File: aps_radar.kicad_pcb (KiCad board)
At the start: 4 copper layers, 122.9 x 53.5 mm, 339 parts, among them J1 TRIG_MUX_OUT, J10 RX3_RX4, J2 RX1_RX2, J3 POWER_IN, J4 Tx_Ant, J5 Rx1_Ant, J6 Rx2_Ant, J7 Rx3_Ant, J8 Rx4_Ant, J9 LMX2491_CONN, SW1 PA_EN, SW2 ON/OFF, U1 HMC717A, U10 HMC951A, U11 OPA192, U12 OPA192, U13 HMC717A, U14 HMC951A, U15 OPA192, U16 OPA192, U17 HMC540S, U18 ASDMB-100MHz, U19 OPA192, U2 HMC951A, U20 HMC431, U21 TQP5523, U22 LMX2491RTWR, U23 LP5900-TL3.3, U24 TPS82140, U25 TPS7A49, U26 LP5900-TL3.0, U27 TPS7A90, U28 TPS7A92, U3 OPA192, U4 OPA192, U5 HMC717A, U6 HMC951A, U7 OPA192, U8 OPA192, U9 HMC717A

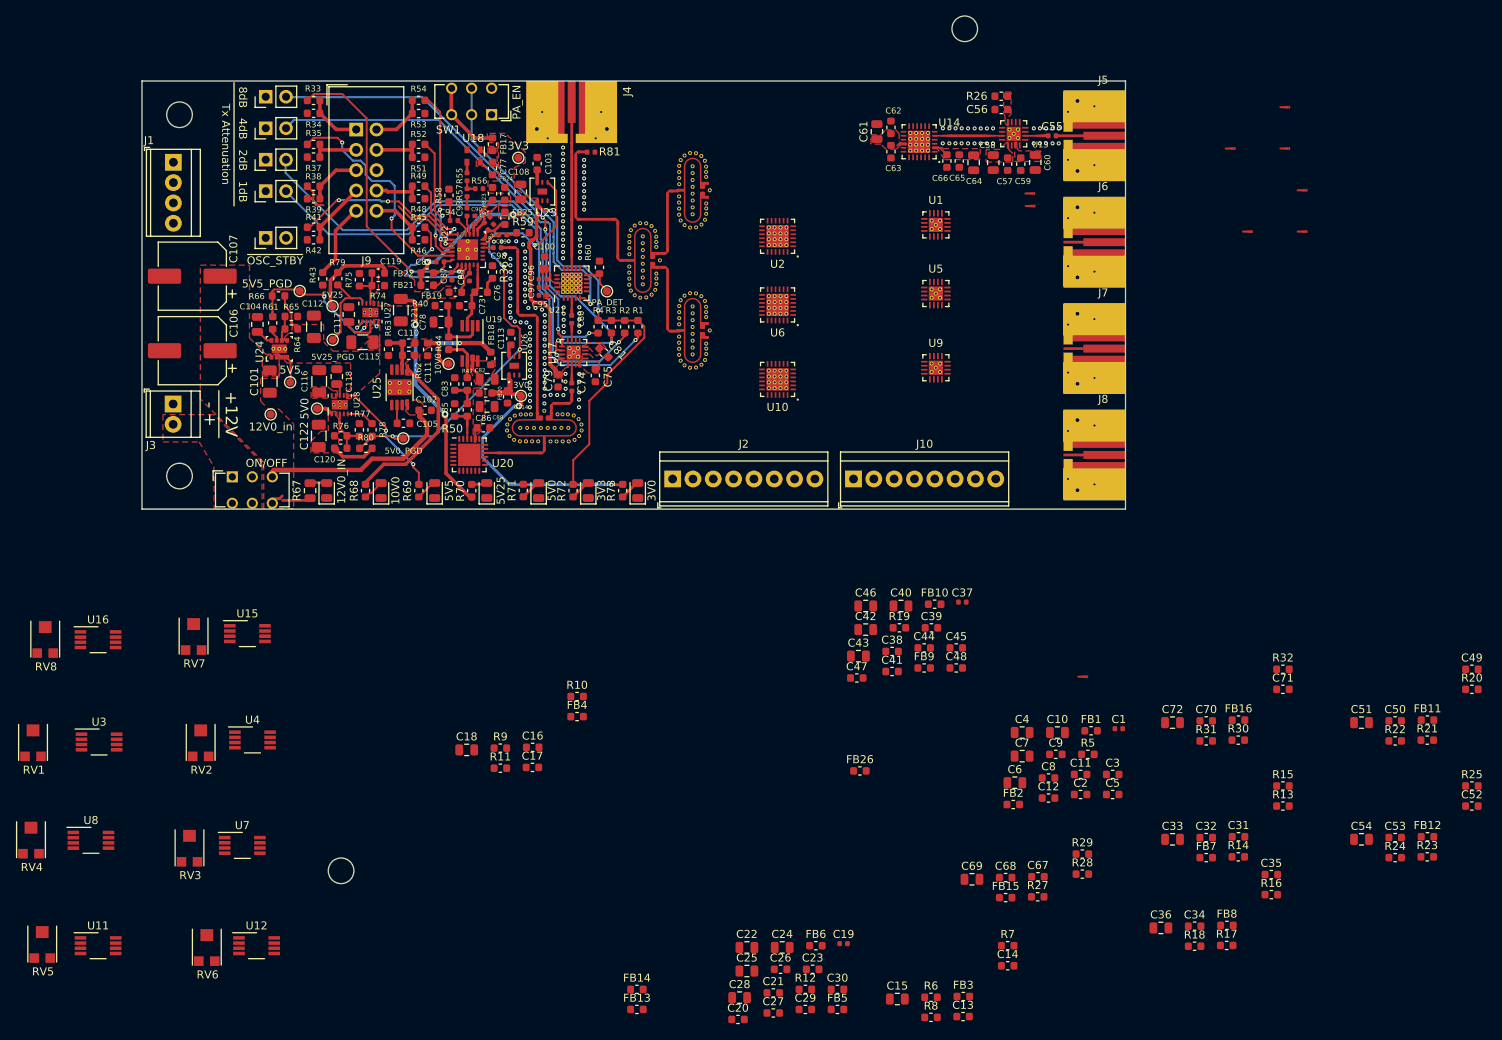
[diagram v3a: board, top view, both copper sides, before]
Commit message: Finished placing parts
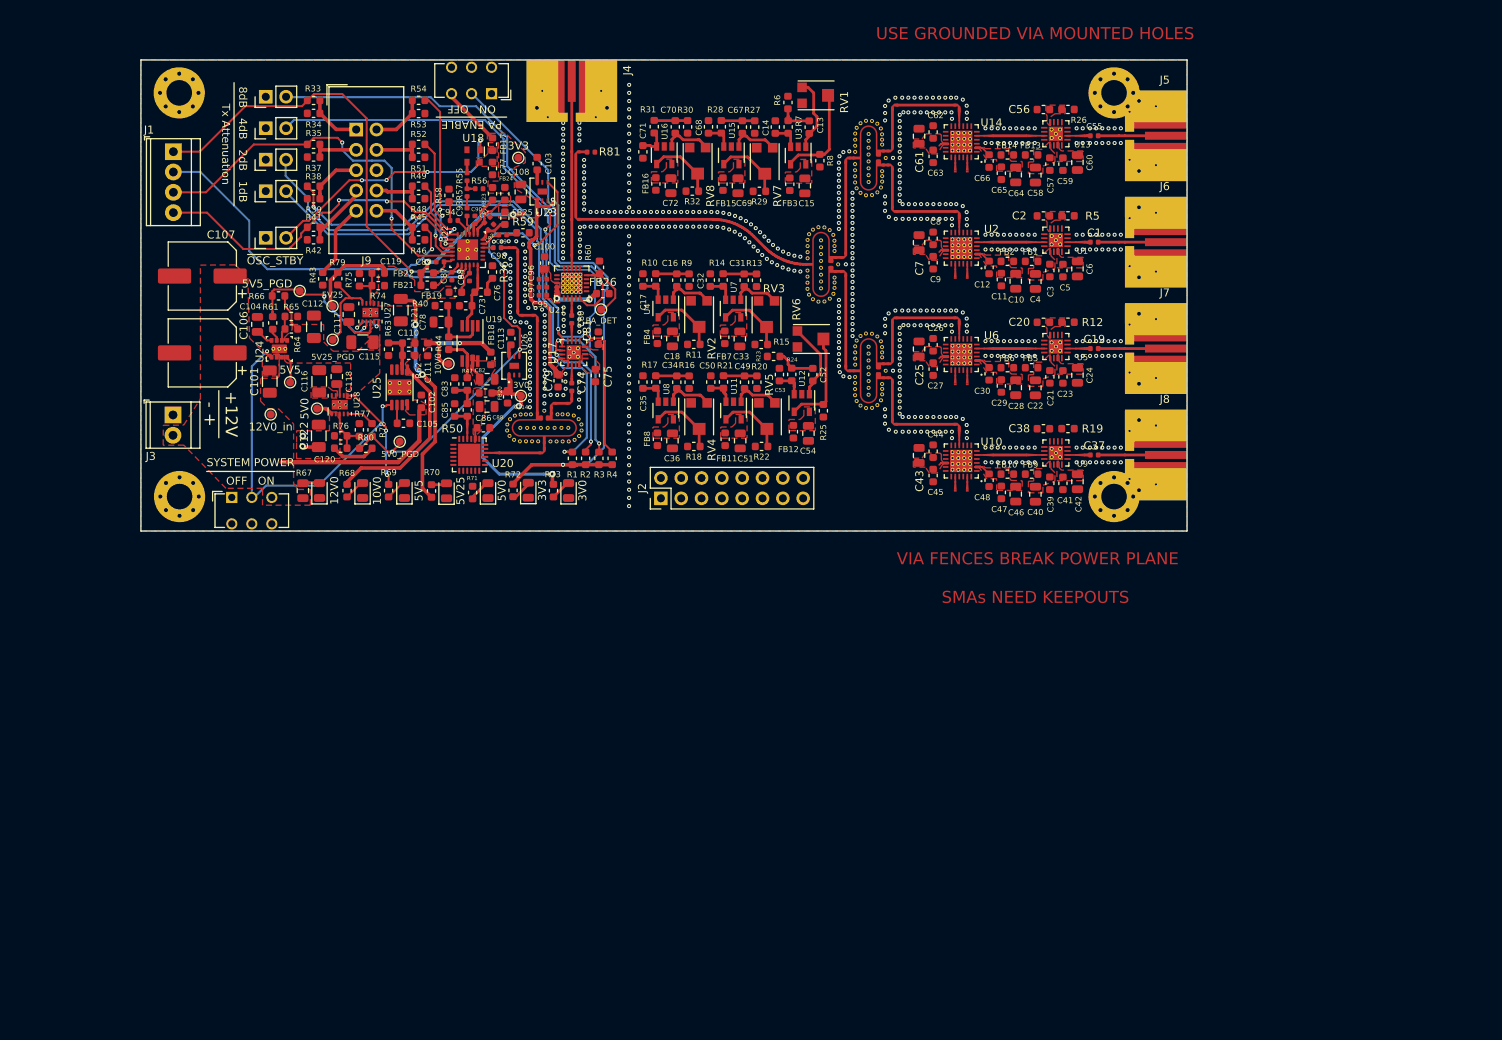
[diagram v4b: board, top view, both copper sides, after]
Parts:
- removed J10: RX3_RX4, TerminalBlock_TE-Connectivity:TerminalBlock_TE_282834-8_1x08_P2.54mm_Horizontal
- added TL37: ic_taper, aps_radar_lib:IC_Taper_0.22_0.35, F.Cu at (198.3, 41.6)
- added TL38: ic_taper, aps_radar_lib:IC_Taper_0.22_0.35, F.Cu at (198.8, 48.7)
- added TL39: ic_taper, aps_radar_lib:IC_Taper_0.22_0.35, F.Cu at (199.8, 54.9)
- added TL40: ic_taper, aps_radar_lib:IC_Taper_0.22_0.35, F.Cu at (198.3, 54.9)
- added TL41: ic_taper, aps_radar_lib:IC_Taper_0.22_0.35, F.Cu at (198.8, 62.0)
- added TL42: ic_taper, aps_radar_lib:IC_Taper_0.22_0.35, F.Cu at (199.8, 68.2)
- added TL43: ic_taper, aps_radar_lib:IC_Taper_0.22_0.35, F.Cu at (198.3, 68.2)
- added TL44: ic_taper, aps_radar_lib:IC_Taper_0.22_0.35, F.Cu at (198.8, 22.1)
- added TL45: ic_taper, aps_radar_lib:IC_Taper_0.22_0.35, F.Cu at (199.8, 28.3)
- added TL46: ic_taper, aps_radar_lib:IC_Taper_0.22_0.35, F.Cu at (198.3, 28.3)
- added TL47: mitered_bend, aps_radar_lib:mitered_bend_50, F.Cu at (198.6, 34.1)
- added TL48: mitered_bend, aps_radar_lib:mitered_bend_50, F.Cu at (198.6, 47.4)
- added TL49: mitered_bend, aps_radar_lib:mitered_bend_50, F.Cu at (198.6, 60.7)
- added TL50: mitered_bend, aps_radar_lib:mitered_bend_50, F.Cu at (198.6, 20.8)
- added TL51: mitered_bend, aps_radar_lib:mitered_bend_50, F.Cu at (190.3, 28.3)
- added TL52: mitered_bend, aps_radar_lib:mitered_bend_50, F.Cu at (190.3, 54.9)
- added TL53: mitered_bend, aps_radar_lib:mitered_bend_50, F.Cu at (190.3, 26.2)
- added TL54: mitered_bend, aps_radar_lib:mitered_bend_50, F.Cu at (190.3, 52.8)
- added TL55: mitered_bend, aps_radar_lib:mitered_bend_50, F.Cu at (190.7, 20.8)
- added TL56: mitered_bend, aps_radar_lib:mitered_bend_50, F.Cu at (190.7, 47.4)
- added TL57: mitered_bend, aps_radar_lib:mitered_bend_50, F.Cu at (190.7, 33.7)
- added TL58: mitered_bend, aps_radar_lib:mitered_bend_50, F.Cu at (190.7, 60.3)
- D1: value 12V0_IN -> 12V0
- H1, H2, H3, H4: footprint MountingHole:MountingHole_3.2mm_M3 -> MountingHole:MountingHole_3.2mm_M3_Pad_Via
- J2: value RX1_RX2 -> IF_OUT; footprint TerminalBlock_TE-Connectivity:TerminalBlock_TE_282834-8_1x08_P2.54mm_Horizontal -> Connector_PinHeader_2.54mm:PinHeader_2x08_P2.54mm_Vertical
- TL23, TL24: value mitered_bend -> ic_taper; footprint aps_radar_lib:mitered_bend_50 -> aps_radar_lib:IC_Taper_0.22_0.35
- U11, U12, U15, U16, U3, U4, U7, U8: footprint Package_SO:VSSOP-8_3.0x3.0mm_P0.65mm -> Package_TO_SOT_SMD:SOT-23-5
- moved RV1 127.0 mm to (181.0, 19.4), turned to 270 degrees
- moved FB13 117.7 mm to (207.9, 26.9)
- moved FB14 114.1 mm to (204.8, 26.9), turned to 180 degrees
- moved U3 114.1 mm to (178.7, 26.9), turned to 270 degrees
- moved R6 113.3 mm to (177.4, 20.3), turned to 90 degrees
- moved C13 112.8 mm to (180.1, 23.4), turned to 90 degrees
- moved RV5 112.0 mm to (174.8, 59.7), turned to 180 degrees
- moved C14 108.8 mm to (175.8, 23.4), turned to 90 degrees
- moved R8 108.0 mm to (181.4, 27.6), turned to 270 degrees
- moved H2 107.3 mm to (218.2, 69.6)
- moved RV6 107.2 mm to (180.4, 49.9), turned to 270 degrees
- moved R7 106.0 mm to (177.4, 23.4), turned to 90 degrees
- moved C71 104.5 mm to (159.3, 26.5), turned to 270 degrees
- moved U11 103.8 mm to (170.6, 58.8), turned to 270 degrees
- moved FB3 103.8 mm to (177.6, 30.5), turned to 90 degrees
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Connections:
- C101 pad 1: /power/+12V0_IN -> /power/+12V0_IN_CONN
- C102 pad 1: /power/+12V0_IN -> /power/+12V0_IN_CONN
- C106 pad 1: /power/+12V0_IN -> /power/+12V0_IN_CONN
- C107 pad 1: /power/+12V0_IN -> /power/+12V0_IN_CONN
- J2 pad 1: /RX1_I -> /RX3_I
- J2 pad 3: /RX1_Q -> GND
- J2 pad 4: GND -> /RX1_I
- J2 pad 5: /RX2_I -> /RX3_Q
- J2 pad 7: /RX2_Q -> GND
- J2 pad 8: GND -> /RX1_Q
- R67 pad 2: /power/+12V0_IN -> /power/+12V0_IN_CONN
- R68 pad 2: (no net) -> +10V
- SW1 pad 5: Net-(SW1-Pad2) -> GND
- SW1 pad 6: +3V3 -> GND
- SW2 pad 1: (no net) -> GND
- SW2 pad 2: /power/+12V0_IN_CONN -> /power/POWER_SW
- SW2 pad 3: /power/+12V0_IN -> /power/+12V0_IN_CONN
- SW2 pad 4: (no net) -> GND
- SW2 pad 5: /power/+12V0_IN_CONN -> GND
- SW2 pad 6: /power/+12V0_IN -> GND
- TL2 pad 1: Net-(TL2-Pad1) -> Net-(TL1-Pad4)
- TL23 pad 1: Net-(TL1-Pad4) -> Net-(TL23-Pad1)
- TL24 pad 1: Net-(TL2-Pad1) -> Net-(TL24-Pad1)
- TL24 pad 2: Net-(TL23-Pad2) -> /receiver_2/IF1_RAW
- TL3 pad 2: /transmitter/LO_1 -> Net-(TL3-Pad2)
- TL3 pad 3: /transmitter/LO_2 -> Net-(TL3-Pad3)
- TL4 pad 2: /transmitter/LO_3 -> Net-(TL4-Pad2)
- TL4 pad 3: /transmitter/LO_4 -> Net-(TL4-Pad3)
- TL5 pad 5: (no net) -> GND
- TP3 pad 1: /power/+12V0_IN -> /power/+12V0_IN_CONN
- U10 pad 10: /transmitter/LO_4 -> Net-(TL41-Pad1)
- U10 pad 20: /receiver_4/IF2_RAW -> Net-(TL43-Pad1)
- U10 pad 23: /receiver_4/IF1_RAW -> Net-(TL42-Pad1)
- U11 pad 1: (no net) -> /RX4_Q
- U11 pad 2: Net-(R22-Pad1) -> GND
- U11 pad 4: GND -> Net-(R22-Pad1)
- U11 pad 5: (no net) -> Net-(C51-Pad1)
- U12 pad 1: (no net) -> /RX4_I
- U12 pad 2: Net-(R25-Pad1) -> GND
- U12 pad 4: GND -> Net-(R25-Pad1)
- U12 pad 5: (no net) -> Net-(C54-Pad1)
- U14 pad 10: /transmitter/LO_1 -> Net-(TL44-Pad1)
- U14 pad 20: /receiver_1/IF2_RAW -> Net-(TL46-Pad1)
- U14 pad 23: /receiver_1/IF1_RAW -> Net-(TL45-Pad1)
- U15 pad 1: (no net) -> /RX1_Q
- U15 pad 2: Net-(R29-Pad1) -> GND
- U15 pad 4: GND -> Net-(R29-Pad1)
- U15 pad 5: (no net) -> Net-(C69-Pad1)
- U16 pad 1: (no net) -> /RX1_I
- U16 pad 2: Net-(R32-Pad1) -> GND
- U16 pad 4: GND -> Net-(R32-Pad1)
- U16 pad 5: (no net) -> Net-(C72-Pad1)
- U2 pad 10: /transmitter/LO_2 -> Net-(TL23-Pad1)
- U2 pad 20: /receiver_2/IF2_RAW -> Net-(TL37-Pad1)
- U2 pad 23: /receiver_2/IF1_RAW -> Net-(TL24-Pad1)
- U24 pad 1: /power/+12V0_IN -> /power/POWER_SW
- U24 pad 2: /power/+12V0_IN -> /power/+12V0_IN_CONN
- U25 pad 5: /power/+12V0_IN -> /power/POWER_SW
- U25 pad 8: /power/+12V0_IN -> /power/+12V0_IN_CONN
- U3 pad 1: (no net) -> /RX2_Q
- U3 pad 2: Net-(R8-Pad1) -> GND
- U3 pad 4: GND -> Net-(R8-Pad1)
- U3 pad 5: (no net) -> Net-(C15-Pad1)
- U4 pad 1: (no net) -> /RX2_I
- U4 pad 2: Net-(R11-Pad1) -> GND
- U4 pad 4: GND -> Net-(R11-Pad1)
- U4 pad 5: (no net) -> Net-(C18-Pad1)
- U6 pad 10: /transmitter/LO_3 -> Net-(TL38-Pad1)
- U6 pad 20: /receiver_3/IF2_RAW -> Net-(TL40-Pad1)
- U6 pad 23: /receiver_3/IF1_RAW -> Net-(TL39-Pad1)
- U7 pad 1: (no net) -> /RX3_Q
- U7 pad 2: Net-(R15-Pad1) -> GND
- U7 pad 4: GND -> Net-(R15-Pad1)
- U7 pad 5: (no net) -> Net-(C33-Pad1)
- U8 pad 1: (no net) -> /RX3_I
- U8 pad 2: Net-(R18-Pad1) -> GND
- U8 pad 4: GND -> Net-(R18-Pad1)
- U8 pad 5: (no net) -> Net-(C36-Pad1)
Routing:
- net /power/POWER_SW: track 0.00 -> 43.6 mm, vias 0 -> 2
- net /LMX_TRIG2: track 16.4 -> 52.9 mm
- net Net-(JP5-Pad2): track 0.00 -> 32.1 mm, vias 0 -> 4
- net /power/+12V0_IN: track 29.7 -> 0.00 mm
- net Net-(TL1-Pad4): track 4.38 -> 30.2 mm
- net /power/+12V0_IN_CONN: track 0.00 -> 22.1 mm
- net /LMX_MOD: track 22.0 -> 42.5 mm
- net /LMX_TRIG1: track 37.4 -> 56.9 mm
- net /LMX_MUXOUT: track 29.6 -> 48.9 mm
- net /~ATTEN_8DB: track 61.3 -> 80.6 mm
- net /~ATTEN_4DB: track 67.9 -> 82.1 mm
- net Net-(R8-Pad1): track 0.00 -> 12.6 mm
- net Net-(R25-Pad1): track 0.00 -> 12.6 mm
- net /transmitter/LMX_CE: track 12.2 -> 22.8 mm, vias 0 -> 2
- net /RX4_I: track 0.00 -> 9.35 mm
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- added copper zone on In2.Cu, net +5V
- added copper zone on B.Cu, net GND
- added copper zone on F.Cu, net GND
- added copper zone on In1.Cu, net GND
- added copper zone on F.Cu, net Net-(C10-Pad1)
- added copper zone on F.Cu, net Net-(C15-Pad1)
- added copper zone on F.Cu, net Net-(C18-Pad1)
- added copper zone on F.Cu, net Net-(C2-Pad1)
- added copper zone on F.Cu, net Net-(C20-Pad1)
- added copper zone on F.Cu, net Net-(C21-Pad1)
- added copper zone on F.Cu, net Net-(C25-Pad1)
- added copper zone on F.Cu, net Net-(C3-Pad1)
- added copper zone on F.Cu, net Net-(C33-Pad1)
- added copper zone on F.Cu, net Net-(C36-Pad1)
- added copper zone on F.Cu, net Net-(C39-Pad1)
- added copper zone on F.Cu, net Net-(C43-Pad1)
- added copper zone on F.Cu, net Net-(C51-Pad1)
- added copper zone on F.Cu, net Net-(C54-Pad1)
- added copper zone on F.Cu, net Net-(C69-Pad1)
- added copper zone on F.Cu, net Net-(C72-Pad1)
- removed copper zone on F.Cu, net /power/+12V0_IN
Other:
- board size 122.9 x 53.5 mm -> 130.8 x 58.9 mm
- net class 50-ohm: clearance 0.32 -> 0.325
- board text added: "OFF ON"
- board text added: "ON OFF"
- board text added: "PA ENABLE"
- board text added: "SMAs NEED KEEPOUTS"
- board text added: "SYSTEM POWER"
- board text added: "USE GROUNDED VIA MOUNTED HOLES"
- board text added: "VIA FENCES BREAK POWER PLANE"

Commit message: Finished layout
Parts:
- added G***: LOGO, aps_radar_lib:spartan_logo, B.Cu at (154.1, 96.4)
- added G***: LOGO, aps_radar_lib:delta_logo, B.Cu at (201.7, 96.5)
- J5: value Rx1_Ant -> Rx1
- J6: value Rx2_Ant -> Rx2
- J7: value Rx3_Ant -> Rx3
- J8: value Rx4_Ant -> Rx4
- U20: footprint Package_DFN_QFN:QFN-24-1EP_4x4mm_P0.5mm_EP2.8x2.8mm -> aps_radar_lib:HMC-LP4
- moved RV6 66.4 mm to (172.6, 115.8), turned to 180 degrees
- moved R6 55.6 mm to (170.4, 75.5), turned to 270 degrees
- moved R23 54.6 mm to (170.9, 106.4), turned to 270 degrees
- moved C4 54.1 mm to (197.1, 95.6)
- moved C10 54.1 mm to (194.6, 95.5)
- moved C46 54.0 mm to (194.7, 122.1)
- moved C22 54.0 mm to (197.1, 108.8)
- moved C28 54.0 mm to (194.7, 108.8)
- moved C40 54.0 mm to (197.1, 122.1)
- moved C58 54.0 mm to (197.1, 82.2)
- moved C64 54.0 mm to (194.7, 82.2)
- moved C73 53.7 mm to (125.9, 98.2)
- moved C76 53.7 mm to (127.8, 96.5)
- moved C108 53.3 mm to (132.8, 83.6)
- moved C111 53.3 mm to (121.2, 103.3)
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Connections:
- H1 pad 1: (no net) -> GND
- H2 pad 1: (no net) -> GND
- H3 pad 1: (no net) -> GND
- H4 pad 1: (no net) -> GND
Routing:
- net GND: track 0.06 -> 95.9 mm, vias 588 -> 1597
- net /receiver_1/IF2_RAW: track 0.00 -> 52.5 mm, vias 0 -> 2
- net /receiver_2/IF2_RAW: track 0.00 -> 52.5 mm, vias 0 -> 2
- net /receiver_4/IF1_RAW: track 0.00 -> 52.5 mm, vias 0 -> 2
- net /receiver_2/IF1_RAW: track 0.00 -> 52.5 mm, vias 0 -> 2
- net /receiver_3/IF2_RAW: track 0.00 -> 52.5 mm, vias 0 -> 2
- net /receiver_4/IF2_RAW: track 0.00 -> 52.5 mm, vias 0 -> 2
- net /receiver_1/IF1_RAW: track 0.00 -> 52.5 mm, vias 0 -> 2
- net /receiver_3/IF1_RAW: track 0.00 -> 51.6 mm, vias 0 -> 2
- net /RX2_Q: track 9.17 -> 59.1 mm, vias 1 -> 2
- net /RX1_Q: track 5.93 -> 54.9 mm, vias 0 -> 2
- net /RX2_I: track 5.81 -> 53.8 mm, vias 0 -> 1
- net /RX3_I: track 5.88 -> 53.9 mm, vias 0 -> 2
- net /RX1_I: track 5.88 -> 53.9 mm, vias 0 -> 1
- net /RX3_Q: track 5.82 -> 53.4 mm, vias 0 -> 1
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- added copper zone on F.Cu, net Net-(C38-Pad1)
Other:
- outline, holes or cut-outs redrawn
- net class 50-ohm: clearance 0.325 -> 0.2
- rule trace_min: 0.2 -> 0.127
- rule via_min_size: 0.3 -> 0.254
- board text added: "DELTA"
- board text added: "Group"
- board text added: "Michigan State University"
- board text added: "Receiver 1"
- board text added: "Receiver 2"
- board text added: "Receiver 3"
- board text added: "Receiver 4"
- board text added: "T1-T2-MUX-MOD"
- board text removed: "SMAs NEED KEEPOUTS"
- board text removed: "USE GROUNDED VIA MOUNTED HOLES"
- board text removed: "VIA FENCES BREAK POWER PLANE"

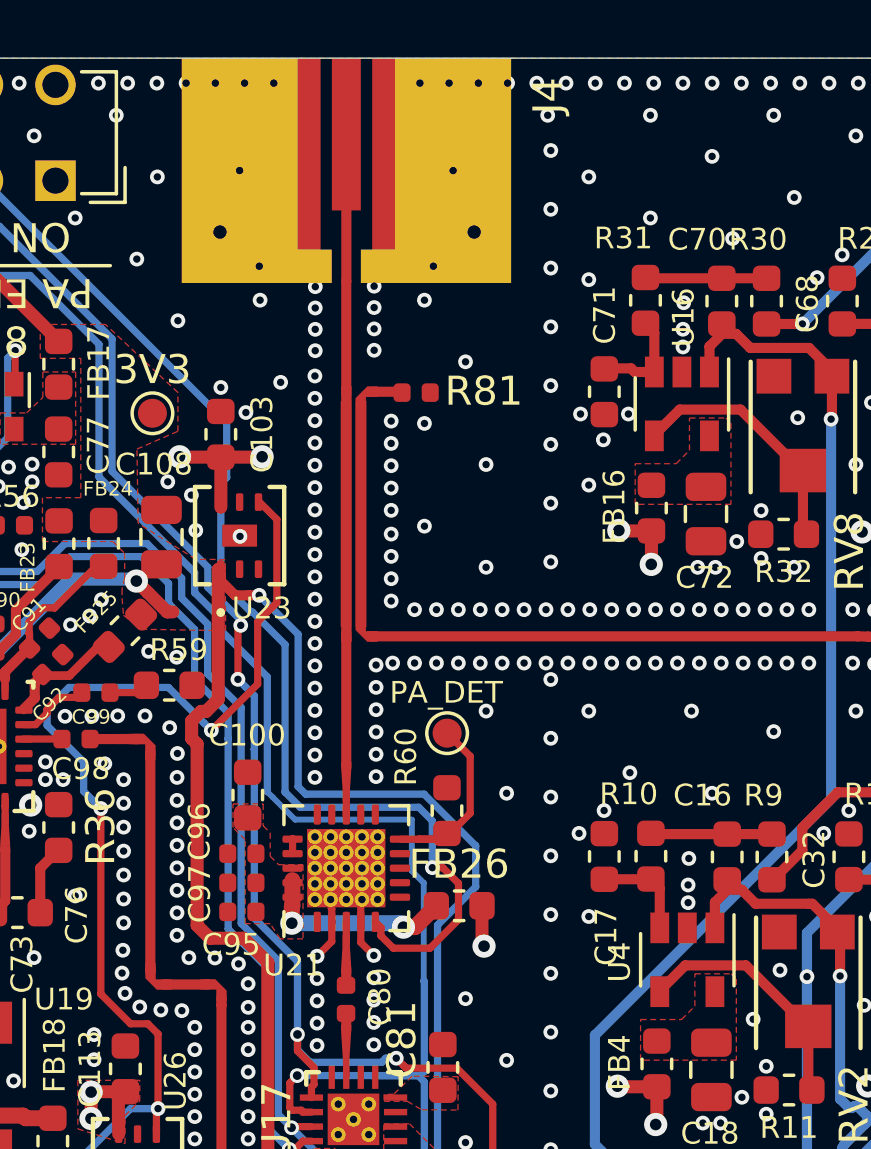
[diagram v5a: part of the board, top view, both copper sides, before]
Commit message: Added SMA model
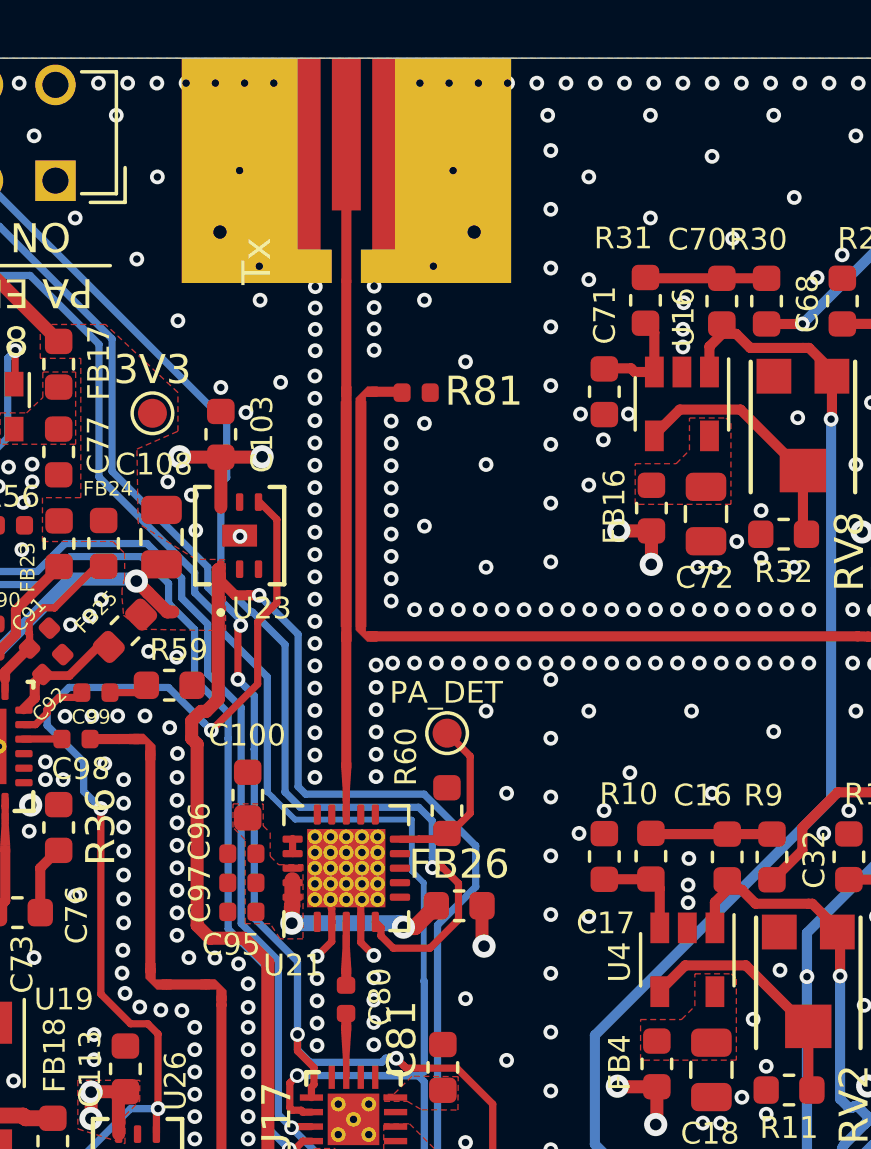
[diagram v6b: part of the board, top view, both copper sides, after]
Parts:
- J4: value Tx_Ant -> Tx
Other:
- board text added: "Revision 1.0"
